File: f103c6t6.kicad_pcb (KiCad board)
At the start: 2 copper layers, 11 parts

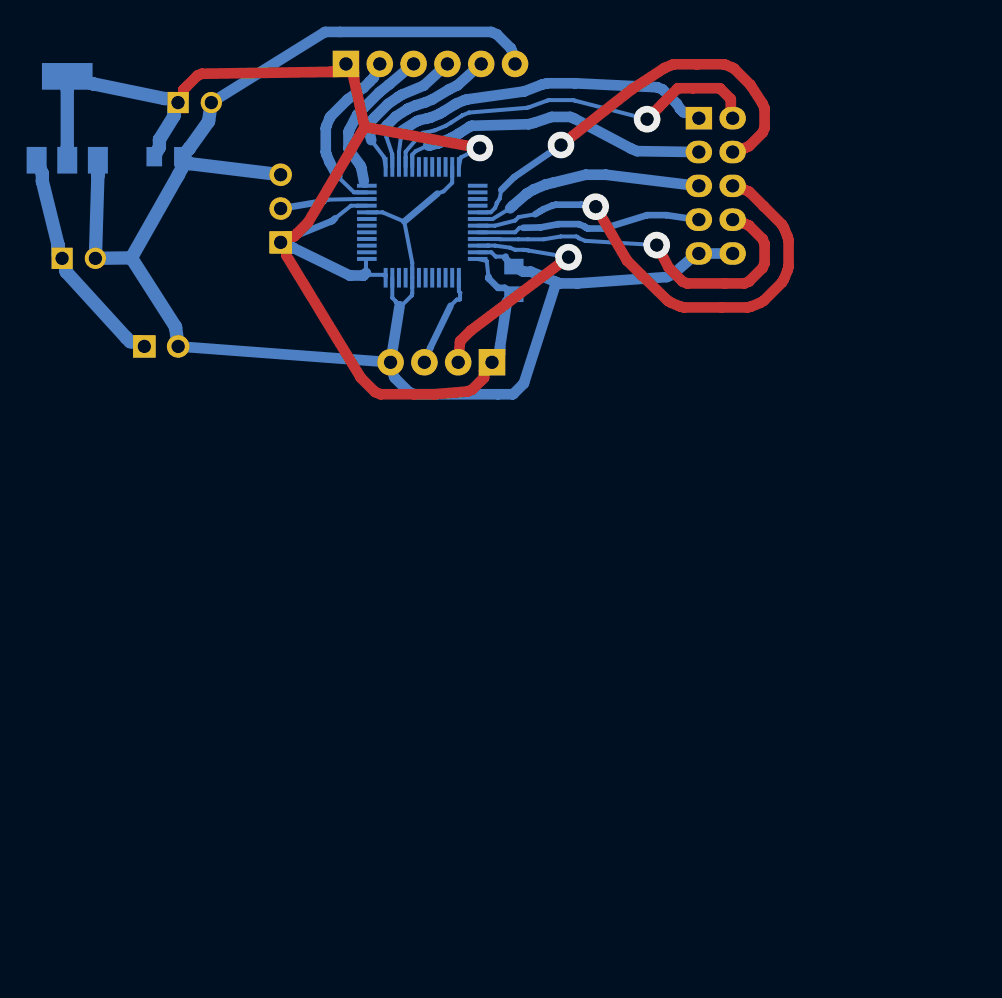
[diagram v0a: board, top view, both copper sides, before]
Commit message: serial +
Добавлен сериал порт для монитора ардуино
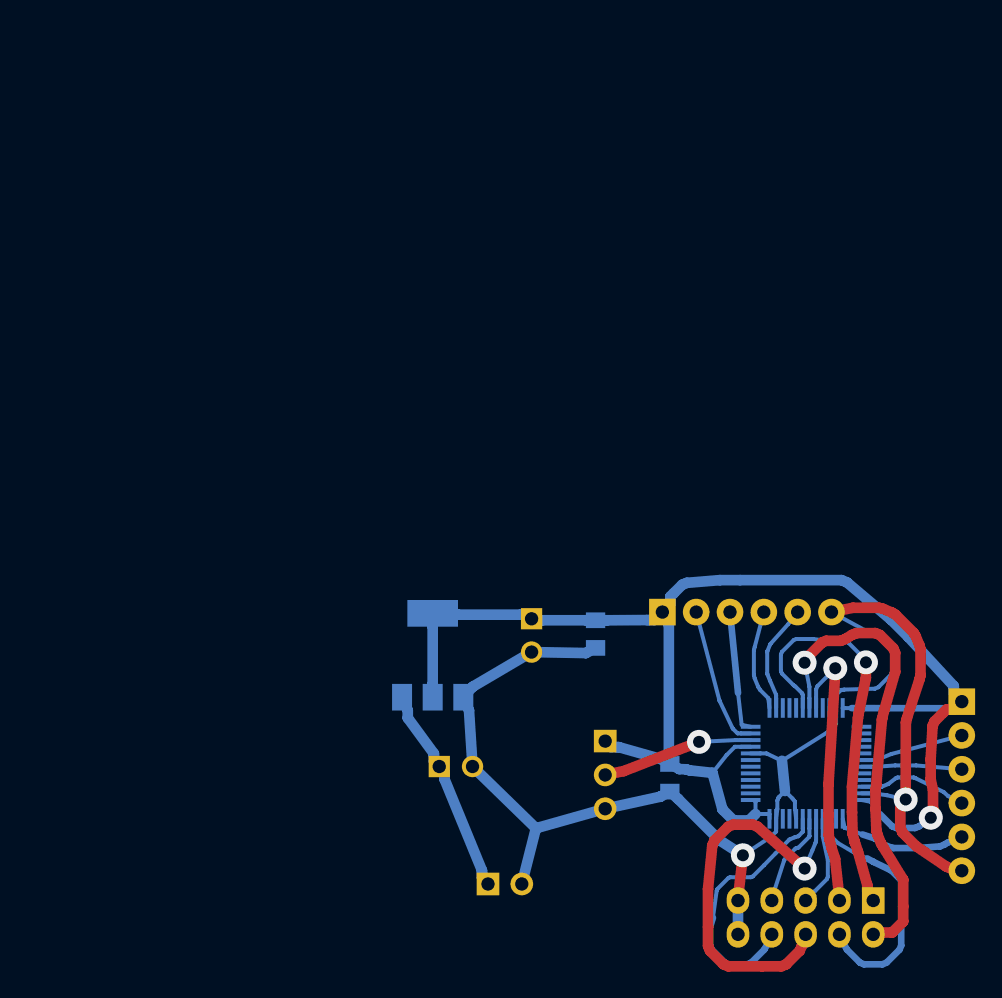
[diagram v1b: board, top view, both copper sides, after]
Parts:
- moved J3 66.9 mm to (162.0, 81.5), turned to 0 degrees
- moved J1 66.5 mm to (155.3, 96.5), turned to -90 degrees
- moved J4 59.7 mm to (126.4, 95.2), turned to 90 degrees
- moved U1 49.8 mm to (150.3, 86.2)
- moved U2 48.8 mm to (122.3, 78.1)
- moved C2 48.1 mm to (134.5, 76.5), turned to -90 degrees
- moved J5 47.5 mm to (139.5, 74.8)
- moved C1 47.5 mm to (122.8, 86.4)
- moved C4 47.0 mm to (129.7, 75.3), turned to -90 degrees
- moved C3 39.2 mm to (140.1, 87.3), turned to -90 degrees
- moved J2 29.7 mm to (135.2, 84.5), turned to 0 degrees
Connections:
- J1 pad 1: +3.3V -> Net-(J1-Pin_1)
- J1 pad 2: RX433 -> Net-(J1-Pin_2)
- J1 pad 3: GNDREF -> Net-(J1-Pin_3)
- J2 pad 2: Net-(J2-Pin_2) -> RX433
- J2 pad 3: Net-(J2-Pin_3) -> GNDREF
- J3 pad 1: +5V -> +3.3V
- J3 pad 2: GNDREF -> Net-(J3-Pin_2)
- J4 pad 1: Net-(J4-Pin_1) -> +5V
- J4 pad 2: Net-(J4-Pin_2) -> GNDREF
- U1 pad 15: Net-(J4-Pin_1) -> unconnected-(U1-PA5-Pad15)
- U1 pad 16: Net-(J4-Pin_2) -> unconnected-(U1-PA6-Pad16)
- U1 pad 17: Net-(J4-Pin_3) -> unconnected-(U1-PA7-Pad17)
- U1 pad 18: unconnected-(U1-PB0-Pad18) -> Net-(J1-Pin_1)
- U1 pad 19: unconnected-(U1-PB1-Pad19) -> Net-(J1-Pin_2)
- U1 pad 20: unconnected-(U1-PB2-Pad20) -> Net-(J1-Pin_3)
- U1 pad 29: Net-(J4-Pin_4) -> unconnected-(U1-PA8-Pad29)
- U1 pad 30: Net-(J4-Pin_5) -> Net-(J3-Pin_2)
- U1 pad 31: Net-(J4-Pin_6) -> Net-(J3-Pin_3)
- U1 pad 32: Net-(J4-Pin_7) -> unconnected-(U1-PA11-Pad32)
- U1 pad 33: Net-(J4-Pin_8) -> unconnected-(U1-PA12-Pad33)
- U1 pad 34: Net-(J2-Pin_2) -> Net-(J3-Pin_4)
- U1 pad 37: Net-(J2-Pin_3) -> Net-(J3-Pin_5)
- U1 pad 39: unconnected-(U1-PB3-Pad39) -> Net-(J1-Pin_4)
- U1 pad 40: unconnected-(U1-PB4-Pad40) -> Net-(J1-Pin_5)
- U1 pad 41: unconnected-(U1-PB5-Pad41) -> Net-(J1-Pin_6)
- U1 pad 42: unconnected-(U1-PB6-Pad42) -> Net-(J1-Pin_7)
- U1 pad 43: unconnected-(U1-PB7-Pad43) -> Net-(J1-Pin_8)
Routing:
- net Net-(J4-Pin_6): track 36.9 -> 0.00 mm, vias 1 -> 0
- net Net-(J1-Pin_2): track 0.00 -> 35.4 mm, vias 0 -> 1
- net Net-(J4-Pin_4): track 32.0 -> 0.00 mm, vias 1 -> 0
- net Net-(J1-Pin_1): track 0.00 -> 30.6 mm, vias 0 -> 1
- net Net-(J4-Pin_2): track 29.7 -> 0.00 mm, vias 1 -> 0
- net Net-(J1-Pin_6): track 0.00 -> 29.7 mm, vias 0 -> 1
- net Net-(J4-Pin_8): track 28.4 -> 0.00 mm, vias 1 -> 0
- net GNDREF: track 143.0 -> 114.7 mm, vias 0 -> 2
- net Net-(J4-Pin_1): track 26.7 -> 0.00 mm
- net Net-(J4-Pin_3): track 23.7 -> 0.00 mm
- net Net-(J1-Pin_3): track 0.00 -> 21.1 mm, vias 0 -> 1
- net Net-(J1-Pin_8): track 0.00 -> 19.8 mm
- net Net-(J1-Pin_4): track 0.00 -> 19.0 mm
- net Net-(J2-Pin_2): track 18.8 -> 0.00 mm, vias 1 -> 0
- net Net-(J4-Pin_5): track 17.6 -> 0.00 mm
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
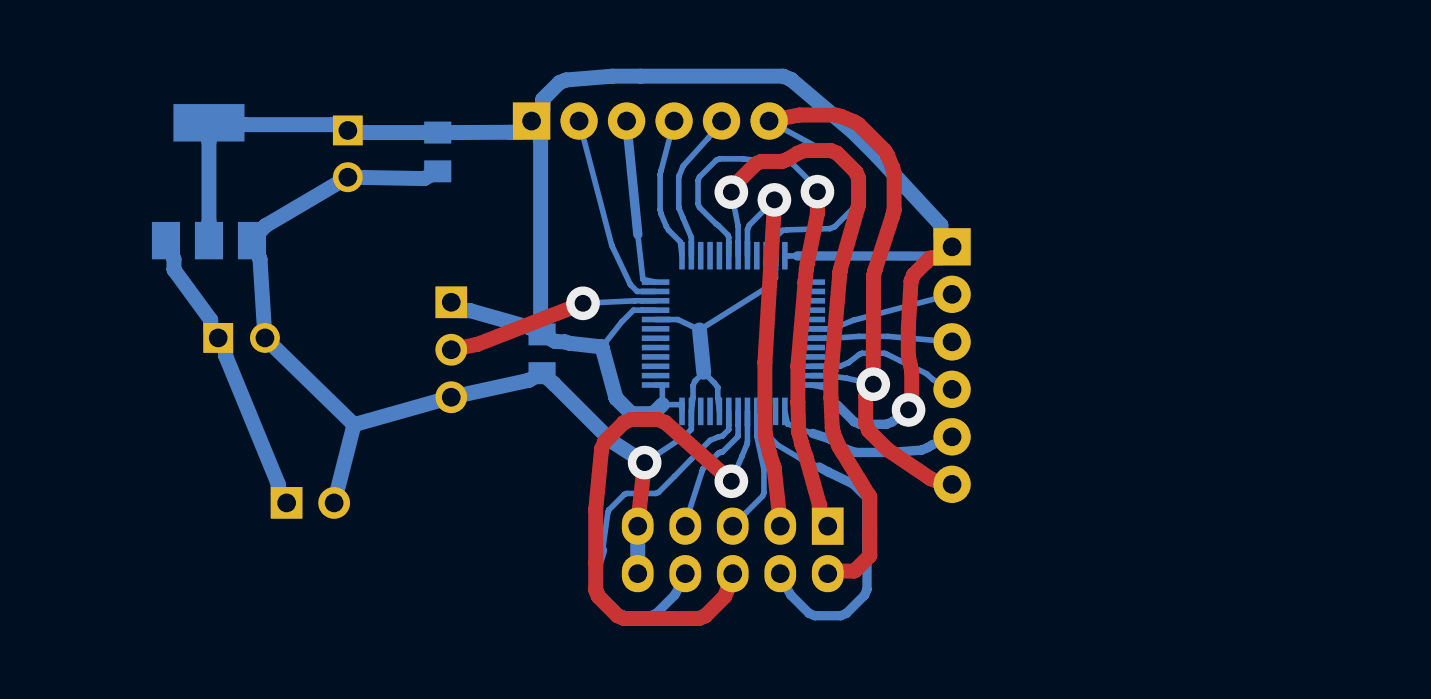
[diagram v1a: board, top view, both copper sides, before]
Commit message: Gerber
Экспортированы слои в гербер и дрил для сверловки
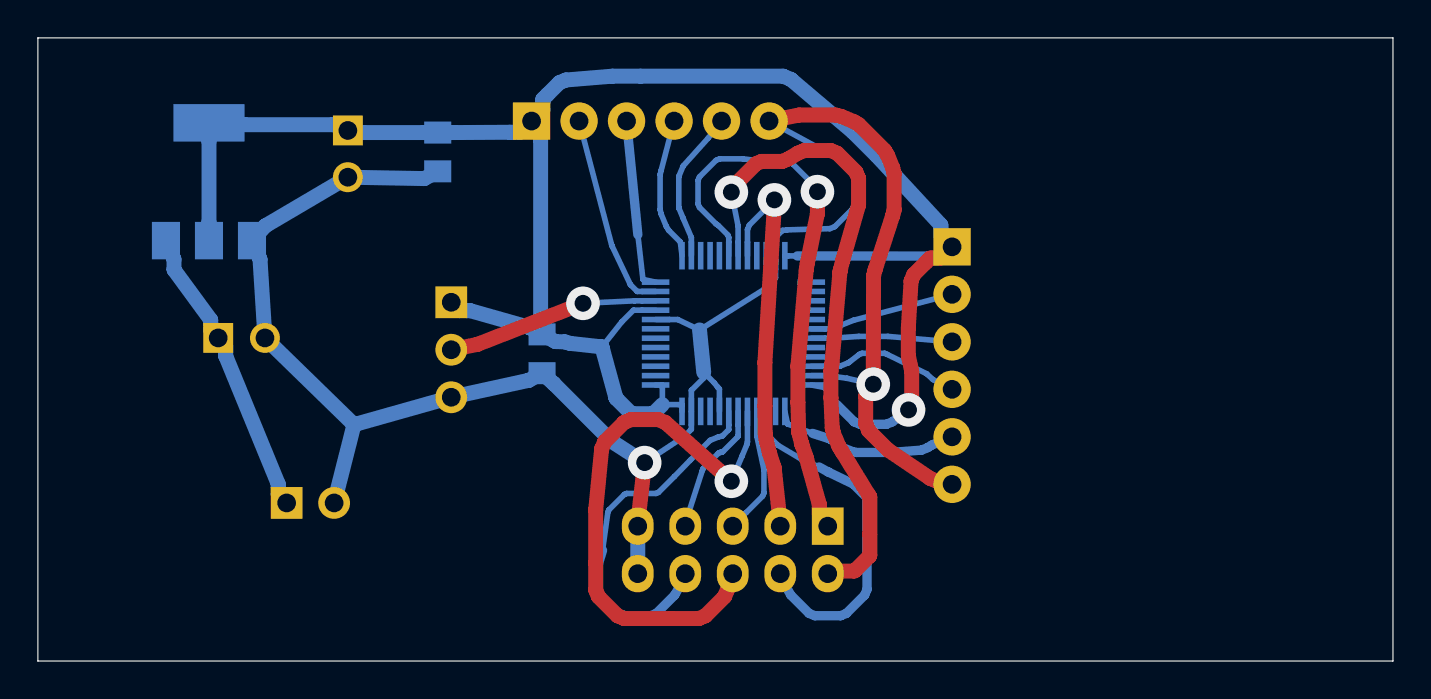
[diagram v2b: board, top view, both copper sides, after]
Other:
- board outline added: 72.5 x 33.3 mm
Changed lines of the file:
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@@
 	)
 	(setup
+		(stackup
+			(layer "F.SilkS"
+				(type "Top Silk Screen")
+			)
+			(layer "F.Paste"
+				(type "Top Solder Paste")
+			)
+			(layer "F.Mask"
+				(type "Top Solder Mask")
+				(thickness 0.01)
+			)
+			(layer "F.Cu"
+				(type "copper")
+				(thickness 0.035)
+			)
+			(layer "dielectric 1"
+				(type "core")
+				(thickness 1.51)
+				(material "FR4")
+				(epsilon_r 4.5)
+				(loss_tangent 0.02)
+			)
+			(layer "B.Cu"
+				(type "copper")
+				(thickness 0.035)
+			)
+			(layer "B.Mask"
+				(type "Bottom Solder Mask")
+				(thickness 0.01)
+			)
+			(layer "B.Paste"
+				(type "Bottom Solder Paste")
+			)
+			(layer "B.SilkS"
+				(type "Bottom Silk Screen")
+			)
+			(copper_finish "None")
+			(dielectric_constraints no)
+		)
 		(pad_to_mask_clearance 0)
 		(allow_soldermask_bridges_in_footprints no)
 		(tenting front back)
 		(pcbplotparams
-			(layerselection 0x00000000_00000000_55555555_57555554)
+			(layerselection 0x00000000_00000000_55555555_57555555)
 			(plot_on_all_layers_selection 0x00000000_00000000_00000000_00000000)
 			(disableapertmacros no)
@@
 			(hpglpenspeed 20)
 			(hpglpendiameter 15.000000)
-			(pdf_front_fp_property_popups no)
-			(pdf_back_fp_property_popups no)
-			(pdf_metadata no)
-			(pdf_single_document yes)
+			(pdf_front_fp_property_popups yes)
+			(pdf_back_fp_property_popups yes)
+			(pdf_metadata yes)
+			(pdf_single_document no)
 			(dxfpolygonmode yes)
 			(dxfimperialunits yes)
 			(dxfusepcbnewfont yes)
-			(psnegative yes)
+			(psnegative no)
 			(psa4output no)
 			(plot_black_and_white yes)
@@
 			(crossoutdnponfab yes)
 			(subtractmaskfromsilk no)
-			(outputformat 4)
+			(outputformat 1)
 			(mirror no)
 			(drillshape 0)
@@
 				(font
 					(size 0.001 0.001)
+					(thickness 0.15)
 				)
 			)
@@
 		(at 155.3463 96.4709 -90)
 		(property "Reference" "J1"
-			(at -1.27 -1.27 -270)
+			(at -1.27 -1.27 90)
 			(unlocked yes)
 			(layer "F.SilkS")
@@
 		)
 		(property "Value" ""
-			(at 0 0 -270)
+			(at 0 0 90)
 			(unlocked yes)
 			(layer "F.SilkS")
@@
 				(font
 					(size 0.001 0.001)
+					(thickness 0.15)
 				)
 			)
@@
 				(font
 					(size 0.001 0.001)
+					(thickness 0.15)
 				)
 			)
@@
 		(at 126.4097 95.2284 90)
 		(property "Reference" "J4"
-			(at 1.27 1.27 -90)
+			(at 1.27 1.27 270)
 			(unlocked yes)
 			(layer "F.SilkS")
@@
 		)
 		(property "Value" ""
-			(at 0 0 -90)
+			(at 0 0 270)
 			(unlocked yes)
 			(layer "F.SilkS")
@@
 				(font
 					(size 0.001 0.001)
+					(thickness 0.15)
 				)
 			)
@@
 		(at 139.5085 74.8059 90)
 		(property "Reference" "J5"
-			(at 1.27 1.27 -90)
+			(at 1.27 1.27 270)
 			(unlocked yes)
 			(layer "F.SilkS")
@@
 		)
 		(property "Value" ""
-			(at 0 0 -90)
+			(at 0 0 270)
 			(unlocked yes)
 			(layer "F.SilkS")
@@
 				(font
 					(size 0.001 0.001)
+					(thickness 0.15)
 				)
 			)
@@
 		(at 129.6838 75.3097 -90)
 		(property "Reference" "C4"
-			(at -1.27 -1.27 -270)
+			(at -1.27 -1.27 90)
 			(unlocked yes)
 			(layer "F.SilkS")
@@
 		)
 		(property "Value" ""
-			(at 0 0 -270)
+			(at 0 0 90)
 			(unlocked yes)
 			(layer "F.SilkS")
@@
 				(font
 					(size 0.001 0.001)
+					(thickness 0.15)
 				)
 			)
@@
 				(font
 					(size 0.001 0.001)
+					(thickness 0.15)
 				)
 			)
@@
 				(font
 					(size 0.001 0.001)
+					(thickness 0.15)
 				)
 			)
@@
 				(font
 					(size 0.001 0.001)
+					(thickness 0.15)
 				)
 			)
@@
 				(font
 					(size 0.001 0.001)
+					(thickness 0.15)
 				)
 			)
@@
 				(font
 					(size 0.001 0.001)
+					(thickness 0.15)
 				)
 			)
@@
 		(end 113.1067 103.7197)
 		(stroke
-			(width 0)
+			(width 0.1)
 			(type solid)
 		)
@@
 		(end 185.597 103.7197)
 		(stroke
-			(width 0)
+			(width 0.1)
 			(type solid)
 		)
@@
 		(end 113.1067 70.3147)
 		(stroke
-			(width 0)
+			(width 0.1)
 			(type solid)
 		)
@@
 		(end 185.597 70.3147)
 		(stroke
-			(width 0)
+			(width 0.1)
 			(type solid)
 		)
 		(layer "Eco2.User")
 	)
+	(gr_rect
+		(start 113.1062 70.358)
+		(end 185.5724 103.6828)
+		(stroke
+			(width 0.05)
+			(type default)
+		)
+		(fill no)
+		(layer "Edge.Cuts")
+	)
 	(segment
 		(start 158.5614 92.3877)
@@
 	)
 	(segment
+		(start 149.2825 88.8108)
+		(end 148.7148 88.2424)
+		(width 0.3)
+		(layer "B.Cu")
+		(net 1)
+	)
+	(segment
+		(start 149.4638 89.04)
+		(end 149.4541 89.0303)
+		(width 0.3)
+		(layer "B.Cu")
+		(net 1)
+	)
+	(segment
 		(start 152.9131 80.6656)
 		(end 152.9238 80.655)
@@
 	)
 	(segment
-		(start 148.1426 88.9542)
-		(end 148.2284 88.747)
-		(width 0.3)
-		(layer "B.Cu")
-		(net 1)
-	)
-	(segment
 		(start 152.5532 82.0077)
 		(end 152.5532 81.2699)
@@
 	)
 	(segment
-		(start 156.6659 79.5113)
-		(end 156.7733 79.2521)
+		(start 149.4541 89.0303)
+		(end 149.2825 88.8108)
 		(width 0.3)
 		(layer "B.Cu")
@@
 	)
 	(segment
-		(start 148.0532 90.3327)
-		(end 148.1426 89.5977)
+		(start 156.6659 79.5113)
+		(end 156.7733 79.2521)
 		(width 0.3)
 		(layer "B.Cu")
@@
 	)
 	(segment
-		(start 148.2284 88.747)
-		(end 148.248 88.7101)
+		(start 149.4638 89.042708)
+		(end 149.4638 89.04)
 		(width 0.3)
 		(layer "B.Cu")
@@
 	)
 	(segment
-		(start 149.4541 89.0303)
-		(end 149.2825 88.8108)
-		(width 0.3)
-		(layer "B.Cu")
-		(net 1)
-	)
-	(segment
-		(start 149.4638 89.5977)
-		(end 149.4638 89.0536)
+		(start 149.5532 90.3327)
+		(end 149.5532 89.132108)
 		(width 0.3)
 		(layer "B.Cu")
@@
 	)
 	(segment
-		(start 148.248 88.7101)
-		(end 148.7148 88.2424)
-		(width 0.3)
-		(layer "B.Cu")
-		(net 1)
-	)
-	(segment
 		(start 152.5532 81.0255)
 		(end 152.9069 80.6718)
@@
 	)
 	(segment
+		(start 149.5532 89.132108)
+		(end 149.4638 89.042708)
+		(width 0.3)
+		(layer "B.Cu")
+		(net 1)
+	)
+	(segment
 		(start 155.465 80.5604)
 		(end 155.7242 80.453)
@@
 	)
 	(segment
-		(start 149.5532 90.3327)
-		(end 149.4638 89.5977)
+		(start 148.7148 88.5466)
+		(end 148.7148 88.2424)
+		(width 0.3)
+		(layer "B.Cu")
+		(net 1)
+	)
+	(segment
+		(start 148.0532 89.2082)
+		(end 148.7148 88.5466)
 		(width 0.3)
 		(layer "B.Cu")
@@
 	)
 	(segment
-		(start 149.2825 88.8108)
-		(end 148.7148 88.2424)
-		(width 0.3)
+		(start 128.9497 95.2284)
+		(end 130.0123 91.0439)
+		(width 0.8)
 		(layer "B.Cu")
 		(net 1)
 	)
 	(segment
-		(start 128.9497 95.2284)
-		(end 130.0123 91.0439)
-		(width 0.8)
+		(start 148.0532 90.3327)
+		(end 148.0532 89.2082)
+		(width 0.3)
 		(layer "B.Cu")
 		(net 1)
@@
 	)
 	(segment
-		(start 149.4638 89.0536)
-		(end 149.4541 89.0303)
-		(width 0.3)
-		(layer "B.Cu")
-		(net 1)
-	)
-	(segment
 		(start 148.7148 88.2424)
 		(end 148.4906 85.9769)
@@
 		(layer "B.Cu")
 		(net 1)
-	)
-	(segment
-		(start 148.1426 89.5977)
-		(end 148.1426 88.9542)
-		(width 0.3)
-		(layer "B.Cu")
-		(net 1)

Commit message: 12.11.2025
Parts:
- moved C2 97.1 mm to (47.0, 34.2)
- moved J1 97.1 mm to (67.9, 54.3)
- moved J2 97.1 mm to (47.7, 42.3)
- moved C1 97.1 mm to (35.3, 44.2)
- moved C4 97.1 mm to (42.2, 33.1)
- moved J3 97.1 mm to (74.5, 39.3)
- moved J4 97.1 mm to (38.9, 53.0)
- moved J5 97.1 mm to (52.0, 32.6)
- moved U1 97.1 mm to (62.8, 44.0)
- moved U2 97.1 mm to (34.8, 35.8)
- moved C3 97.1 mm to (52.6, 45.0)
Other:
- board size 72.5 x 33.3 mm -> 47.5 x 33.3 mm

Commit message: Оптимизация
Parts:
- C1: value (none) -> C_Polarized; footprint C1 -> Capacitor_THT:CP_Radial_D7.5mm_P2.50mm
- C2: value (none) -> C_Small; footprint C2 -> Capacitor_SMD:C_0805_2012Metric_Pad1.18x1.45mm_HandSolder
- C3: value (none) -> C_Small; footprint C3 -> Capacitor_SMD:C_0805_2012Metric_Pad1.18x1.45mm_HandSolder
- C4: value (none) -> C_Polarized; footprint C4 -> Capacitor_THT:CP_Radial_D7.5mm_P2.50mm
- J1: value (none) -> Conn_01x10_Pin; footprint J1 -> main:PinHeader_2x05_P2.54mm_Vertical
- J2: value (none) -> Conn_01x03_Pin; footprint J2 -> main:PinHeader_1x03_P2.54mm_Vertical
- J3: value (none) -> Conn_01x06_Pin; footprint J3 -> main:PinHeader_1x06_P2.54mm_Vertical
- J4: value (none) -> Conn_01x02_Pin; footprint J4 -> main:PinHeader_1x02_P2.54mm_Vertical
- J5: value (none) -> Conn_01x06_Pin; footprint J5 -> main:PinHeader_1x06_P2.54mm_Vertical
- U1: value (none) -> STM32F103C6Tx; footprint U1 -> Package_QFP:LQFP-48_7x7mm_P0.5mm
- U2: value (none) -> AMS1117-3.3; footprint U2 -> Package_TO_SOT_SMD:SOT-223-3_TabPin2
- moved J3 6.71 mm to (67.9, 38.4)
- moved U1 5.71 mm to (57.1, 44.0), turned to 0 degrees
- moved U2 5.22 mm to (39.8, 34.6), turned to 90 degrees
- moved J1 4.91 mm to (63.1, 55.4)
- moved C3 3.99 mm to (49.3, 47.3), turned to 90 degrees
- moved C4 3.48 mm to (45.7, 33.0)
- moved J2 2.87 mm to (45.4, 43.9)
- moved C2 2.56 mm to (49.5, 33.8), turned to 90 degrees
- moved C1 2.35 mm to (37.6, 44.6)
- moved J4 2.28 mm to (36.9, 54.2)
- moved J5 0.51 mm to (52.5, 32.5)
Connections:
- net Net-(J3-Pin_2) renamed /TX
- net Net-(J3-Pin_3) renamed /RX
- net Net-(J3-Pin_4) renamed /SWDIO
- net Net-(J3-Pin_5) renamed /SWCLK
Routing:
- net GNDREF: track 114.8 -> 141.4 mm, vias 2 -> 0
- net +3.3V: track 109.7 -> 93.1 mm
- net Net-(J1-Pin_2): track 35.4 -> 30.9 mm
- net RX433: track 11.4 -> 15.6 mm, vias 1 -> 0
- net button_4: track 8.14 -> 11.8 mm
- net Net-(J1-Pin_6): track 29.7 -> 26.2 mm
- net button_3: track 7.66 -> 10.8 mm
- net button_1: track 10.7 -> 13.6 mm
- net button_2: track 9.20 -> 11.9 mm
- net Net-(J1-Pin_1): track 30.6 -> 28.3 mm
- net Net-(J1-Pin_4): track 19.0 -> 20.7 mm
- net /SWDIO: track 8.23 -> 7.01 mm
- net /SWCLK: track 9.98 -> 8.82 mm
- net Net-(J1-Pin_5): track 6.90 -> 8.04 mm
- net Net-(J1-Pin_3): track 21.1 -> 22.1 mm
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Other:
- board size 47.5 x 33.3 mm -> 39.4 x 33.3 mm
